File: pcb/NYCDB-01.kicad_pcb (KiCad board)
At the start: 2 copper layers, 263 parts, among them J1 AUDIO_JACK, J2 AUDIO_JACK, P1 CONN_BATT, P2 USB_OTG, Q1 Q_PMOS_GSD, SW1 SW_POWER, SW2 SW_RESET, U1 CS5361, U10 OPA4134, U11 TPA6120A2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

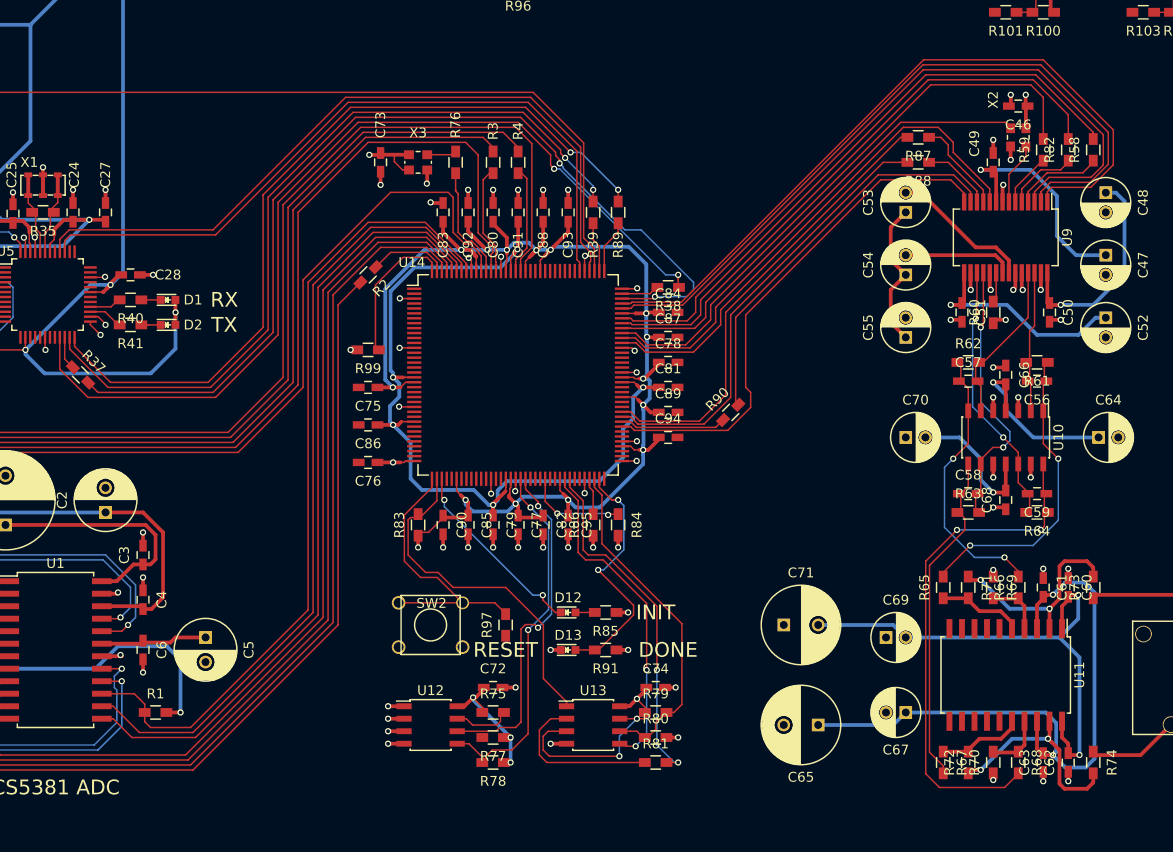
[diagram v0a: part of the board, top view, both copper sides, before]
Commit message: Cleaned up DRC errors from new 0603 footprints
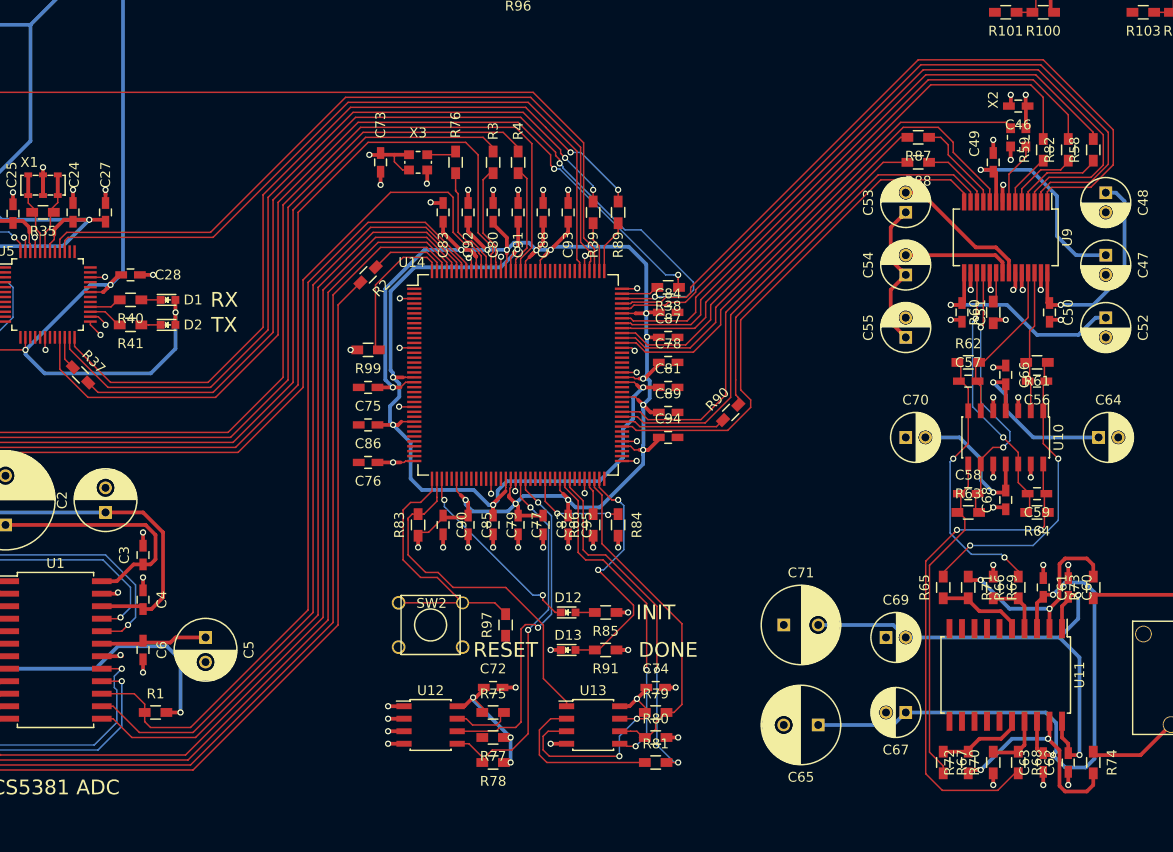
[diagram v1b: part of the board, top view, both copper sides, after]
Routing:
- net GND: track 191.7 -> 194.0 mm
- net Net-(R97-Pad2): track 28.9 -> 29.6 mm
- net Net-(R71-Pad1): track 21.4 -> 21.9 mm

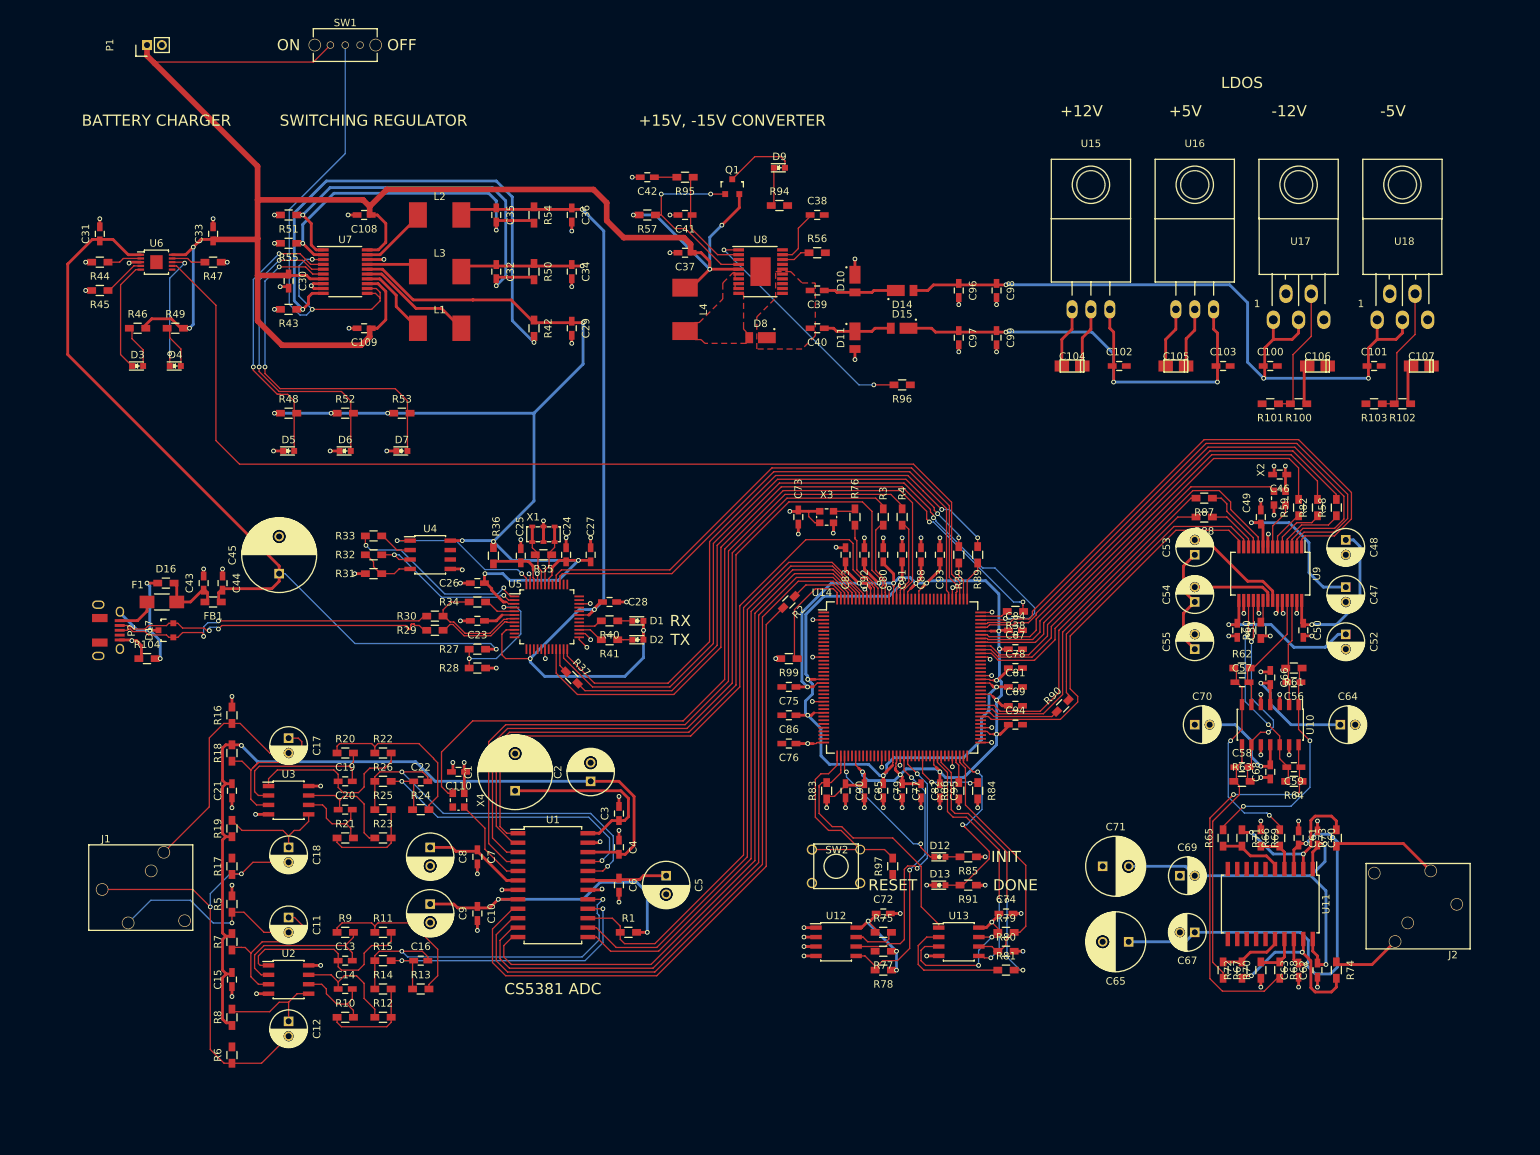
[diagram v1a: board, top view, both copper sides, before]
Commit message: Added a ground plane
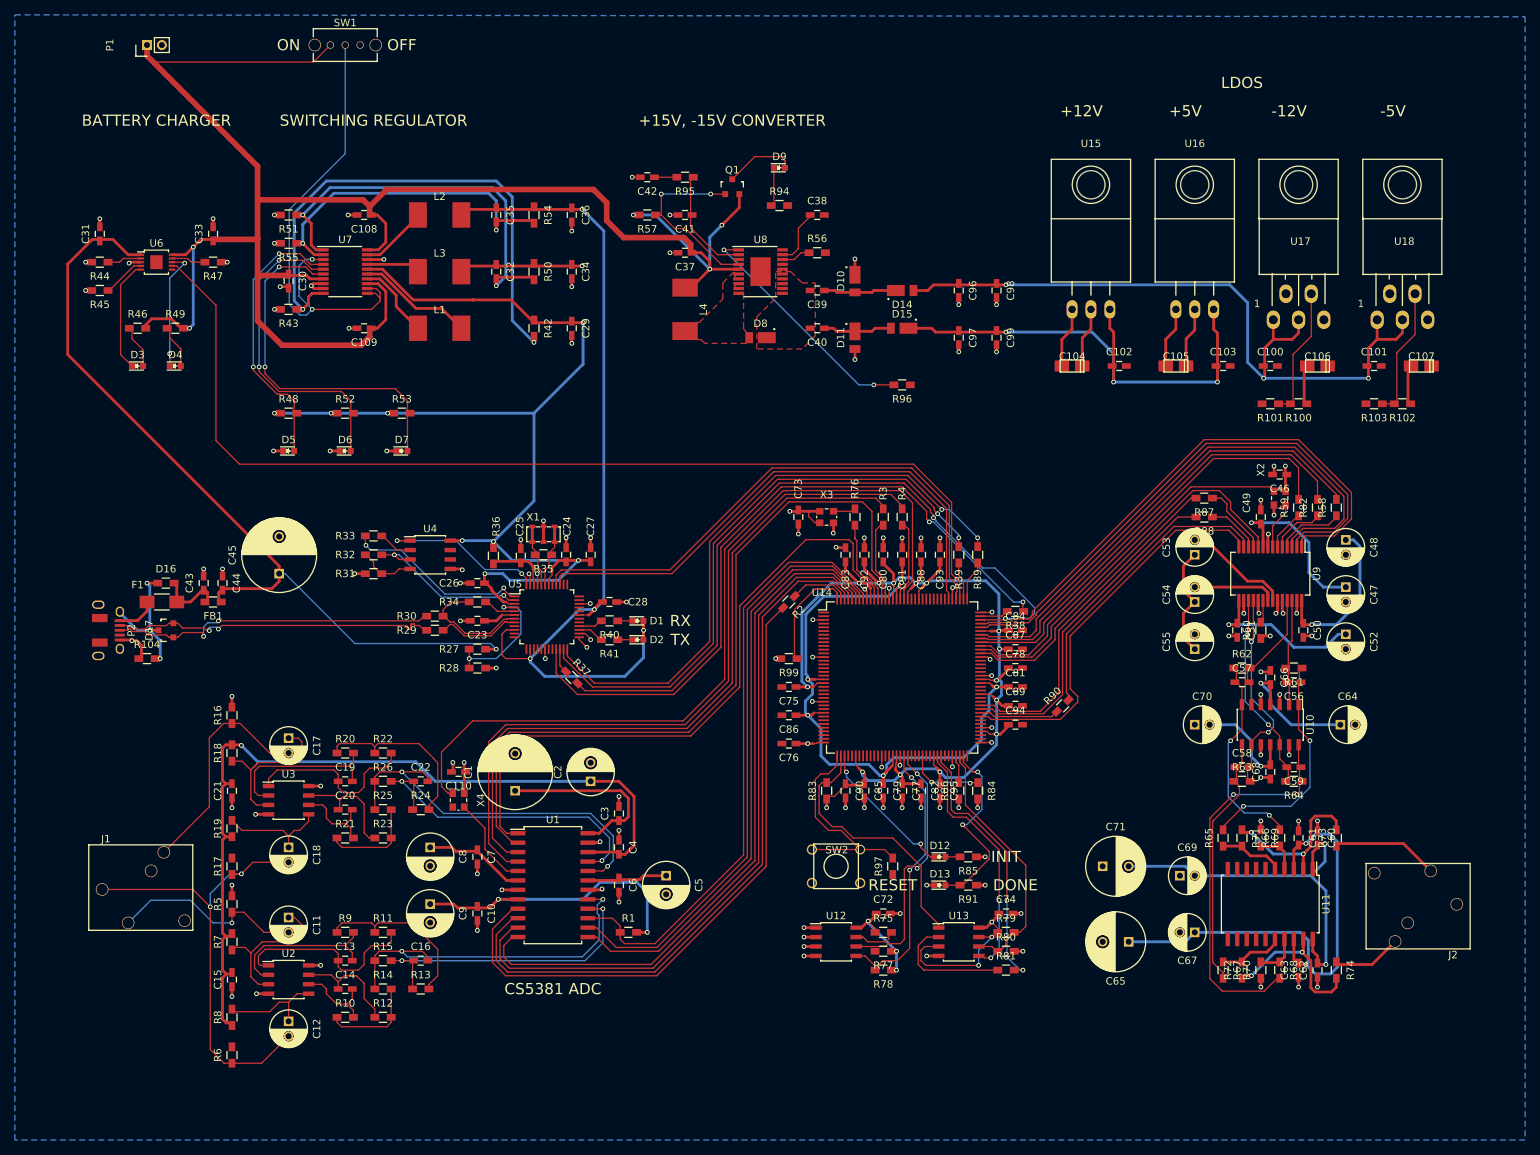
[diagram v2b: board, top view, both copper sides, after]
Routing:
- added copper zone on B.Cu, net GND
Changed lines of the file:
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@@
     (links 625)
     (no_connects 226)
-    (area 0 0 0 0)
+    (area 19.469099 13.409742 208.9024 155.847401)
     (thickness 1.6)
     (drawings 16)
@@
       )
     )
+  )
+  (zone (net 2) (net_name GND) (layer B.Cu) (hatch edge 0.508)
+    (connect_pads (clearance 0.508))
+    (min_thickness 0.254)
+    (fill yes (arc_segments 16) (thermal_gap 0.508) (thermal_bridge_width 0.508))
+    (polygon
+      (pts
+        (xy 215.9 13.97) (xy 215.9 165.1) (xy 12.7 165.1) (xy 12.7 13.716)
+      )
+    )

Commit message: Added some missing ground vias
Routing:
- net GND: track 194.0 -> 199.2 mm, vias 121 -> 125
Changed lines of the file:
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@@
     (links 625)
     (no_connects 226)
-    (area 19.469099 13.409742 208.9024 155.847401)
+    (area 12.7 13.409742 215.900001 165.100001)
     (thickness 1.6)
     (drawings 16)
-    (tracks 2453)
+    (tracks 2461)
     (zones 0)
     (modules 263)
@@
   (segment (start 94.736 122.12) (end 95.25 121.606) (width 0.381) (layer F.Cu) (net 1))
   (segment (start 93.98 122.12) (end 94.736 122.12) (width 0.381) (layer F.Cu) (net 1) (status 10))
+  (segment (start 148.27 109.22) (end 149.606 109.22) (width 0.381) (layer F.Cu) (net 2))
+  (via (at 149.606 109.22) (size 0.635) (drill 0.381) (layers F.Cu B.Cu) (net 2))
+  (segment (start 148.27 106.68) (end 149.606 106.68) (width 0.381) (layer F.Cu) (net 2))
+  (via (at 149.606 106.68) (size 0.635) (drill 0.381) (layers F.Cu B.Cu) (net 2))
+  (segment (start 148.27 104.14) (end 149.606 104.14) (width 0.381) (layer F.Cu) (net 2))
+  (via (at 149.606 104.14) (size 0.635) (drill 0.381) (layers F.Cu B.Cu) (net 2))
+  (segment (start 148.27 101.6) (end 149.606 101.6) (width 0.381) (layer F.Cu) (net 2))
+  (via (at 149.606 101.6) (size 0.635) (drill 0.381) (layers F.Cu B.Cu) (net 2))
+  (segment (start 124.46 85.41) (end 123.256 85.41) (width 0.381) (layer F.Cu) (net 2))
+  (segment (start 123.256 85.41) (end 123.19 85.344) (width 0.381) (layer F.Cu) (net 2))
+  (via (at 123.19 85.344) (size 0.635) (drill 0.381) (layers F.Cu B.Cu) (net 2))
+  (segment (start 180.34 80.33) (end 180.34 78.994) (width 0.381) (layer F.Cu) (net 2))
+  (via (at 180.34 78.994) (size 0.635) (drill 0.381) (layers F.Cu B.Cu) (net 2))
   (segment (start 187.96 123.51) (end 187.96 122.174) (width 0.381) (layer F.Cu) (net 2))
   (via (at 187.96 122.174) (size 0.635) (drill 0.381) (layers F.Cu B.Cu) (net 2))
@@
   (segment (start 185.42 142.99) (end 185.42 144.526) (width 0.381) (layer F.Cu) (net 2))
   (via (at 185.42 144.526) (size 0.635) (drill 0.381) (layers F.Cu B.Cu) (net 2))
-  (segment (start 180.34 80.53) (end 180.34 78.994) (width 0.381) (layer F.Cu) (net 2))
-  (via (at 180.34 78.994) (size 0.635) (drill 0.381) (layers F.Cu B.Cu) (net 2))
   (segment (start 118.11 82.03) (end 118.11 83.566004) (width 0.381) (layer F.Cu) (net 2))
   (via (at 118.11 83.566004) (size 0.635) (drill 0.381) (layers F.Cu B.Cu) (net 2))
@@
   (segment (start 127 85.41) (end 127 84.074) (width 0.381) (layer F.Cu) (net 2))
   (via (at 127 84.074) (size 0.635) (drill 0.381) (layers F.Cu B.Cu) (net 2))
-  (segment (start 124.46 85.41) (end 123.256 85.41) (width 0.381) (layer F.Cu) (net 2))
-  (segment (start 123.256 85.41) (end 123.19 85.344) (width 0.381) (layer F.Cu) (net 2))
-  (via (at 123.19 85.344) (size 0.635) (drill 0.381) (layers F.Cu B.Cu) (net 2))
   (segment (start 74.93 135.57) (end 74.93 136.906) (width 0.381) (layer F.Cu) (net 2) (status 10))
   (via (at 74.93 136.906) (size 0.635) (drill 0.381) (layers F.Cu B.Cu) (net 2))

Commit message: Tightened up the LDOs a bit
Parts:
- moved R100 5.39 mm to (189.2, 62.2)
- moved R102 5.39 mm to (203.2, 62.2)
- moved R101 4.58 mm to (184.2, 62.2)
- moved R103 4.58 mm to (198.1, 62.2)
- moved C104 4.02 mm to (156.2, 57.1)
- moved C105 4.02 mm to (170.2, 57.1)
- moved C102 3.81 mm to (161.3, 57.1)
- moved C103 3.81 mm to (175.3, 57.1)
- moved C100 3.59 mm to (184.2, 58.4), turned to 180 degrees
- moved C101 3.59 mm to (198.1, 58.4), turned to 180 degrees
- moved C106 2.84 mm to (189.2, 58.4)
- moved C107 2.84 mm to (203.2, 58.4)
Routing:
- net -15V: track 99.3 -> 30.7 mm, vias 3 -> 2
- net +15V: track 66.8 -> 22.6 mm, vias 3 -> 2
- net GND: track 199.2 -> 182.8 mm
- net -5VA: track 19.9 -> 23.6 mm, vias 1 -> 2
- net -12VA: track 61.1 -> 64.8 mm, vias 4 -> 5
- net Net-(R102-Pad2): track 18.1 -> 14.6 mm
- net Net-(R100-Pad2): track 18.1 -> 14.6 mm
- net +5VA: track 26.2 -> 23.3 mm, vias 1 -> 2
- net +12VA: track 76.3 -> 73.4 mm, vias 4 -> 5

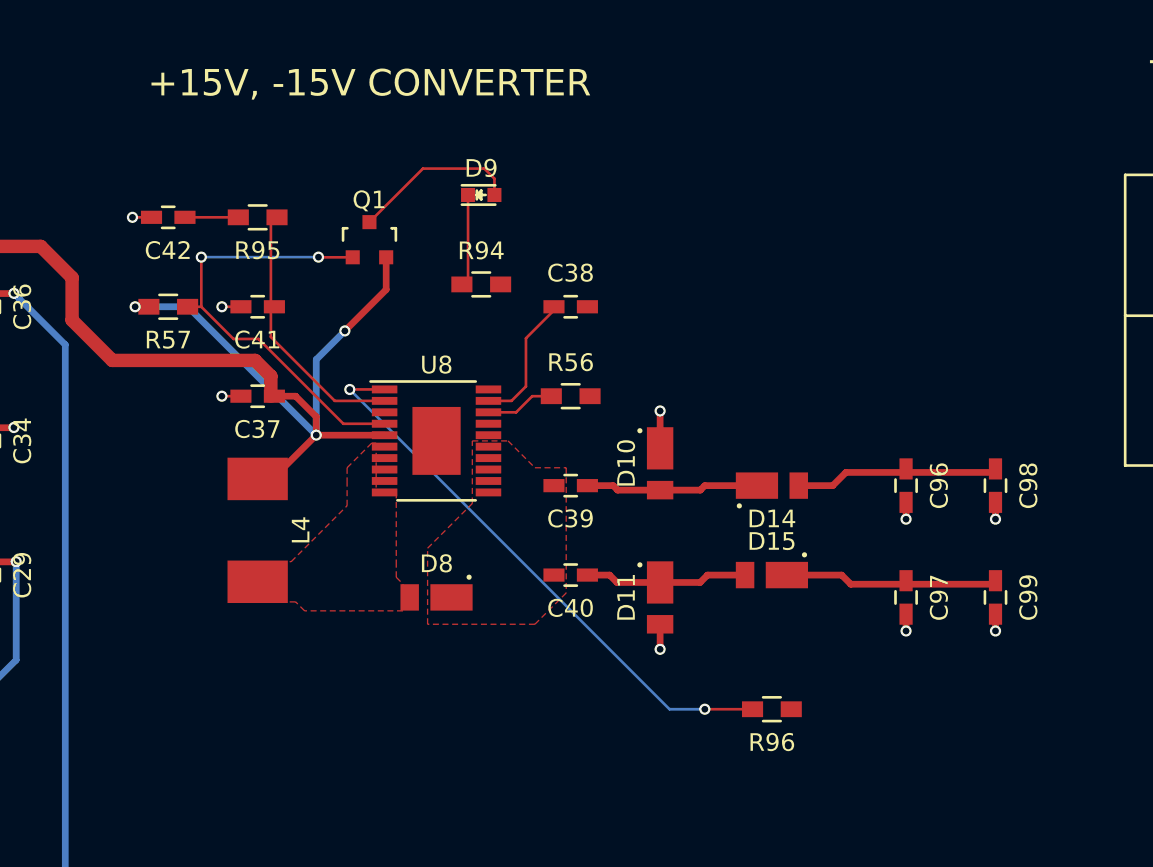
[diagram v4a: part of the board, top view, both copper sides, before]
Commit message: Tightened up the inverting regulator a bit
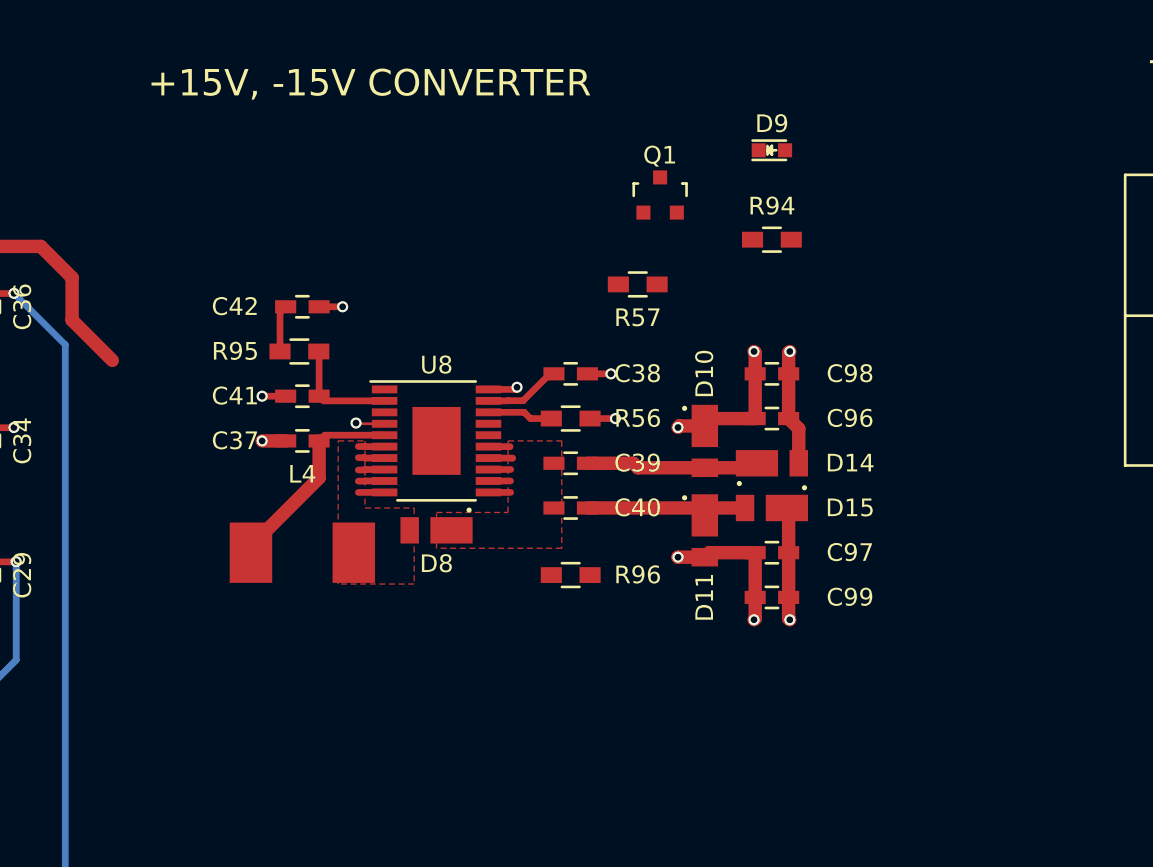
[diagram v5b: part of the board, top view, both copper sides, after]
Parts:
- moved R57 26.7 mm to (124.5, 39.4)
- moved D9 16.7 mm to (132.1, 31.8)
- moved R94 16.7 mm to (132.1, 36.8)
- moved Q1 16.7 mm to (125.7, 34.3)
- moved C98 14.2 mm to (132.1, 44.5), turned to 180 degrees
- moved R96 13.7 mm to (120.7, 55.9)
- moved C99 12.7 mm to (132.1, 57.1), turned to 180 degrees
- moved C42 9.16 mm to (105.4, 40.6), turned to 0 degrees
- moved C96 8.52 mm to (132.1, 47.0), turned to 180 degrees
- moved C97 8.03 mm to (132.1, 54.6), turned to 180 degrees
- moved R95 7.98 mm to (105.2, 43.2)
- moved C41 5.68 mm to (105.4, 45.7)
- moved D11 4.58 mm to (128.3, 53.3)
- moved C38 3.81 mm to (120.7, 44.5)
- moved C40 3.81 mm to (120.7, 52.1)
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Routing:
- net /Power Supplies/V_BATT: track 251.5 -> 211.0 mm, vias 5 -> 2
- net Net-(R96-Pad2): track 32.7 -> 0.00 mm, vias 2 -> 0
- net Net-(Q1-Pad1): track 25.7 -> 1.64 mm, vias 2 -> 1
- net GND: track 182.8 -> 196.0 mm, vias 125 -> 126
- net Net-(D9-Pad2): track 9.52 -> 0.00 mm
- net Net-(C41-Pad1): track 14.8 -> 6.38 mm
- net Net-(D8-Pad2): track 0.00 -> 7.50 mm
- net Net-(C39-Pad2): track 0.00 -> 6.38 mm
- net +15V: track 22.6 -> 17.0 mm, vias 2 -> 3
- net Net-(D9-Pad1): track 5.08 -> 0.00 mm
- net -15V: track 30.7 -> 25.8 mm, vias 2 -> 3
- net Net-(C38-Pad1): track 7.73 -> 4.36 mm
- net Net-(C42-Pad1): track 3.58 -> 2.67 mm
- net Net-(R56-Pad1): track 4.30 -> 3.72 mm
